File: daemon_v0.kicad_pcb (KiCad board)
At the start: 4 copper layers, 86 x 53 mm, 338 parts, among them J1 Battery PTC 2A Fuse, J10 USB-A♂ Charge Port 4, J11 USB-C♀ Main Port 5, J12 WAGO 4P Field Terminal, J13 USB-C♀ Goobay Bridge, J14 RJ45 MagJack, J15 TRRS 3.5mm Jack, J16 Speaker JST, J17 Analog-In, J2 10mΩ Current Sense, J3 40-Pin Radxa Header, J4 AUX GPIO Breakout, J6 ST7789 SPI Display, J7 USB-C♂ Plug → Radxa (KEY), J8 USB-A♀ Host Port 2, J9 USB-A♀ Host Port 3, K1 G6K-2F-Y, Q1 BC857 Dummy Load PNP, Q2 BSS84 Wake PMOS, Q3 2N7002 PMIC Kill NMOS, Q4 AO3400A IR Drive NMOS, Q5 AO3400A, SW1 Power Button, SW2 5-Way Nav Switch, U1 IP5328P PMIC, U10 MAX98357A I2S Amp, U11 ISO1212 Dual Isolator, U12 ESD USB Port1, U13 INMP441 Mic Left, U14 SL2.1A USB Hub 2, U15 SY6280 Port4 USB-A♂, U16 ESD USB Port2, U17 ESD USB Port3, U18 ESD USB Port4, U19 ESD USB Port5, U2 AP2112K 3.3V LDO, U20 ESD Goobay Bridge, U21 PCF8574 I2C GPIO Exp, U22 SY6280 Port5 USB-C♀, U23 3.3→5V Level Shifter, U24 INMP441 Mic Right, U25 ESD9B5.0ST5G, U26 ESD9B5.0ST5G, U27 NAU88C22, U28 ADS1115, U29 SP3485, U3 SL2.1A USB Hub 1, U30 TSOP38238, U31 ATECC608B, U32 74LVC04A, U33 TS3USB221, U34 TS3USB221, U35 TS3USB221, U36 TS3USB221, U37 TS3USB221, U4 SY6280 Port1 Radxa Key, U5 SY6280 Port2 USB-A♀, U6 SY6280 Port3 USB-A♀, U7 NE555 Heartbeat Timer, U8 CC1101 Sub-GHz Radio, U9 RTL8152B Ethernet, Y1 12MHz Hub1 Xtal, Y2 12MHz Hub2 Xtal, Y3 27MHz CC1101 Xtal, Y4 25MHz Ethernet Xtal

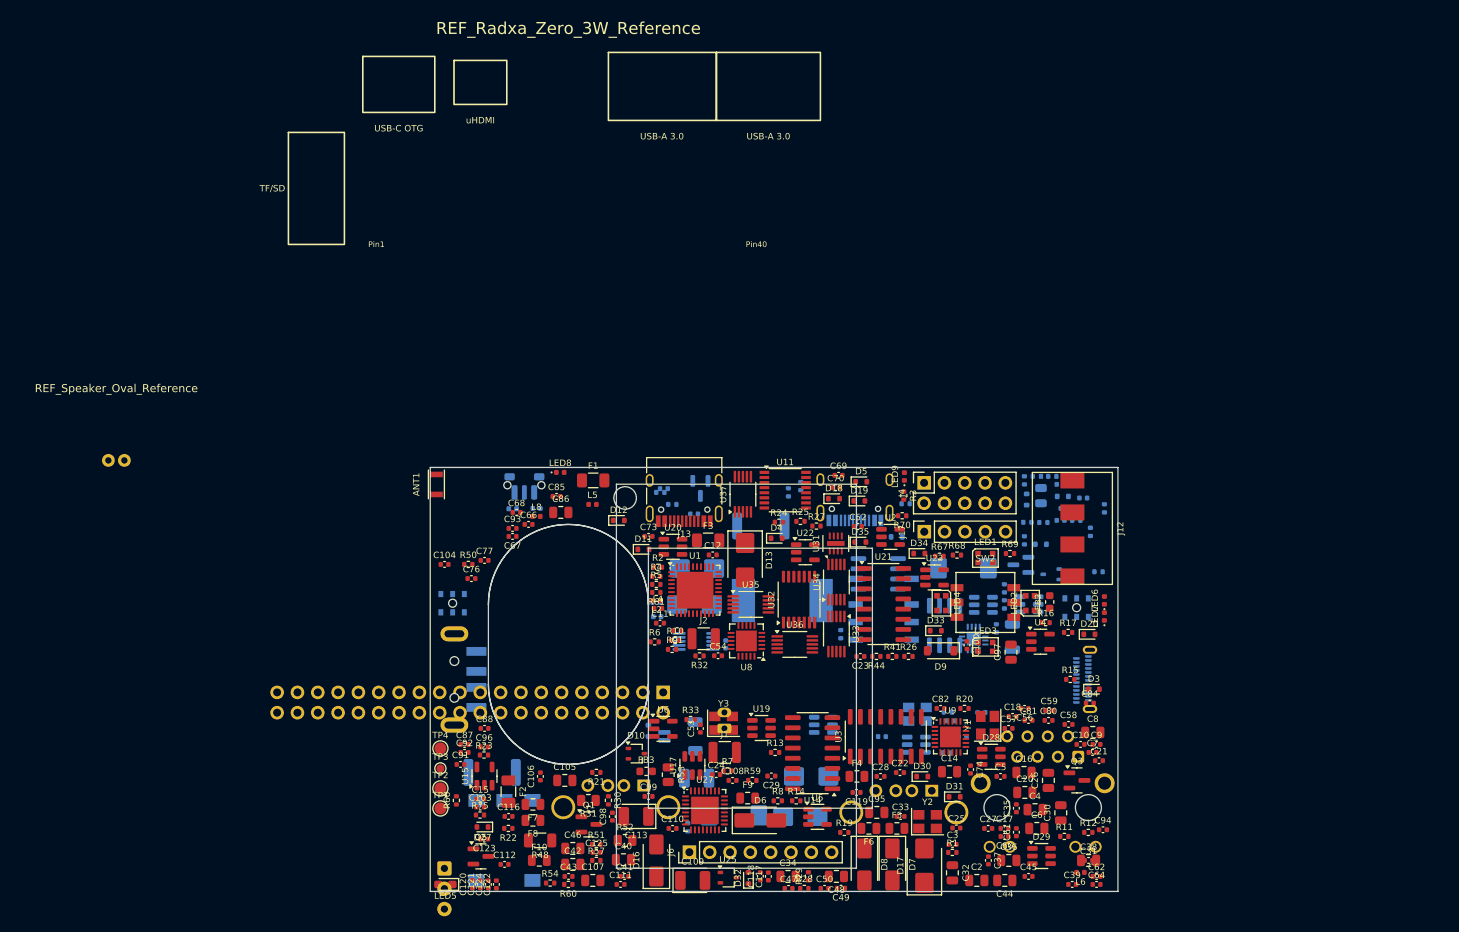
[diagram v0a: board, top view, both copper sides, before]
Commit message: feat: board ready for routing — 4-layer, 336 components, all placed
- 4 copper layers: F.Cu, In1.Cu (GND), In2.Cu (PWR), B.Cu
- All 336 components placed from screenshot4 (0 in staging)
- 1095 pad-net connections
- Mill-Max footprint for J6 screen (bare holes, no 3D model)
- WAGO 3D model linked

Set design rules in KiCad GUI before routing:
  Board Setup → Design Rules → Net Classes:
  - Clearance: 0.15mm
  - Track width: 0.2mm (signal), 0.4mm (power)
  - Via: 0.6mm pad / 0.3mm drill
  Board Setup → Board Stackup → 4 layers

Co-Authored-By: Claude Opus 4.6 (1M context) <noreply@anthropic.com>
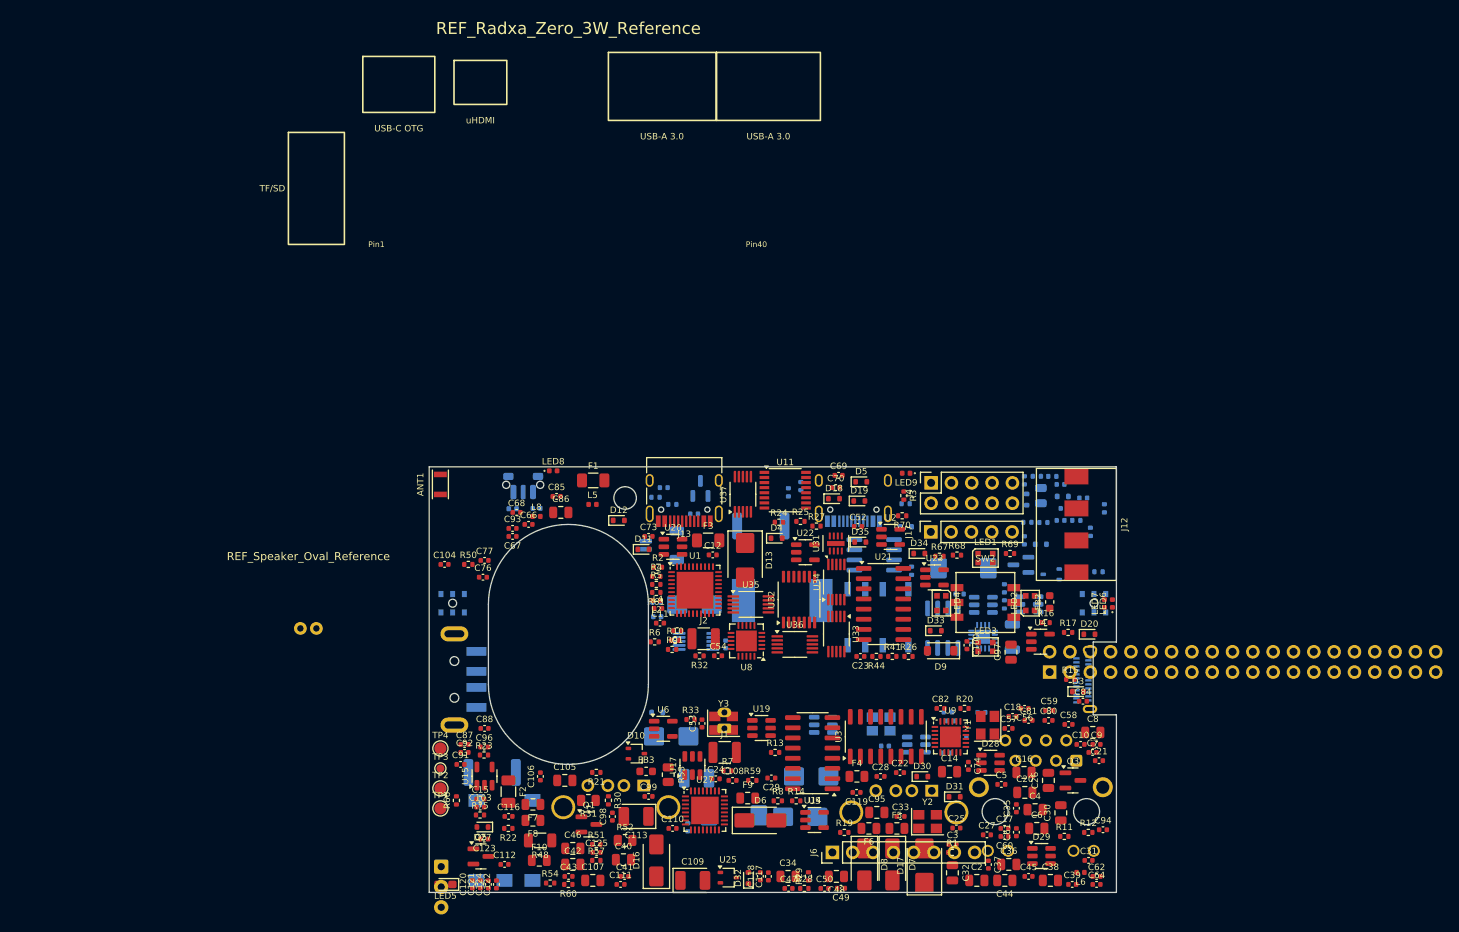
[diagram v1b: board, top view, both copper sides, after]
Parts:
- J6: footprint PinHeader_1x08_P2.54mm_Vertical -> MillMax_1x08_P2.54mm_Vertical
- moved J3 48.4 mm to (142.7, 125.5), turned to -90 degrees
- moved REF_Speaker_Oval_Reference 31.9 mm to (50.0, 120.0)
- moved J16 24.0 mm to (94.2, 109.6)
- moved D14 21.2 mm to (95.3, 133.5), turned to 0 degrees
- moved J6 17.9 mm to (115.5, 148.0)
- moved R18 11.9 mm to (125.4, 112.8), turned to -90 degrees
- moved R43 6.30 mm to (131.4, 115.7), turned to 180 degrees
- moved C38 5.39 mm to (142.8, 151.5)
- moved Y4 4.70 mm to (121.6, 131.9)
- moved D22 2.55 mm to (93.6, 130.5), turned to 0 degrees
- moved U7 2.44 mm to (120.7, 110.8)
- moved U24 2.24 mm to (148.2, 116.8)
- moved D3 2.00 mm to (146.2, 127.9)
- moved D21 1.72 mm to (124.7, 107.3)
- moved LED7 1.63 mm to (149.5, 116.9)
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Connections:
- J12 pad 2: ISO_VCC1 -> WAGO_COM1
- J12 pad 3: WAGO_COM1 -> WAGO_COM2
- J12 pad 4: WAGO_COM2 -> (no net)
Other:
- board size 86 x 53 mm -> 85.9 x 53.2 mm
- board text removed: "54.0 mm"
- board text removed: "⚙️ INDUSTRIAL ISO"
- board text removed: "⚡ POWER"
- board text removed: "🌐 ETHERNET"
- board text removed: "🎮 CONTROL"
- board text removed: "💡 LEDs + IR"
- board text removed: "📍 TEST POINTS"
- board text removed: "📡 RF (keep away from power!)"
- board text removed: "🔀 USB HUB"
- board text removed: "🔊 AUDIO"
- board text removed: "🔌 CONNECTORS"
- board text removed: "🔌 STINGER SWITCHES"
- board text removed: "🔧 TRANSISTORS"
